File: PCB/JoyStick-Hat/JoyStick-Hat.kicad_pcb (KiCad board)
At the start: 2 copper layers, 65 x 100 mm, 108 parts, among them J1 20021121-00010C4LF, J10 Conn_01x02_Pin, J11 Conn_01x02_Pin, J12 Conn_01x02_Pin, J13 Conn_01x02_Pin, J14 Conn_01x03_Pin, J15 Conn_01x03_Pin, J16 Conn_01x06, J2 BU2032SM-JJ-GTR, J3 0675031020, J4 Conn_02x14_Counter_Clockwise, J5 Conn_02x14_Counter_Clockwise, J6 1757242, J7 Raspberry_Pi_2_3, J8 Conn_01x04_Pin, J9 Conn_01x04_Pin, M1 D24V22F12, M2 D24V22F5, M3 D24V22F3, SW1 TL3301NF260QG, U1 STM32F446VETx, U2 TLC5947DAP, U3 TLC5947DAP, U4 MAX3535ECWI+T, X1 ABM3B-8.000MHZ-B2-T, X2 ABS07-32.768KHZ-9-T

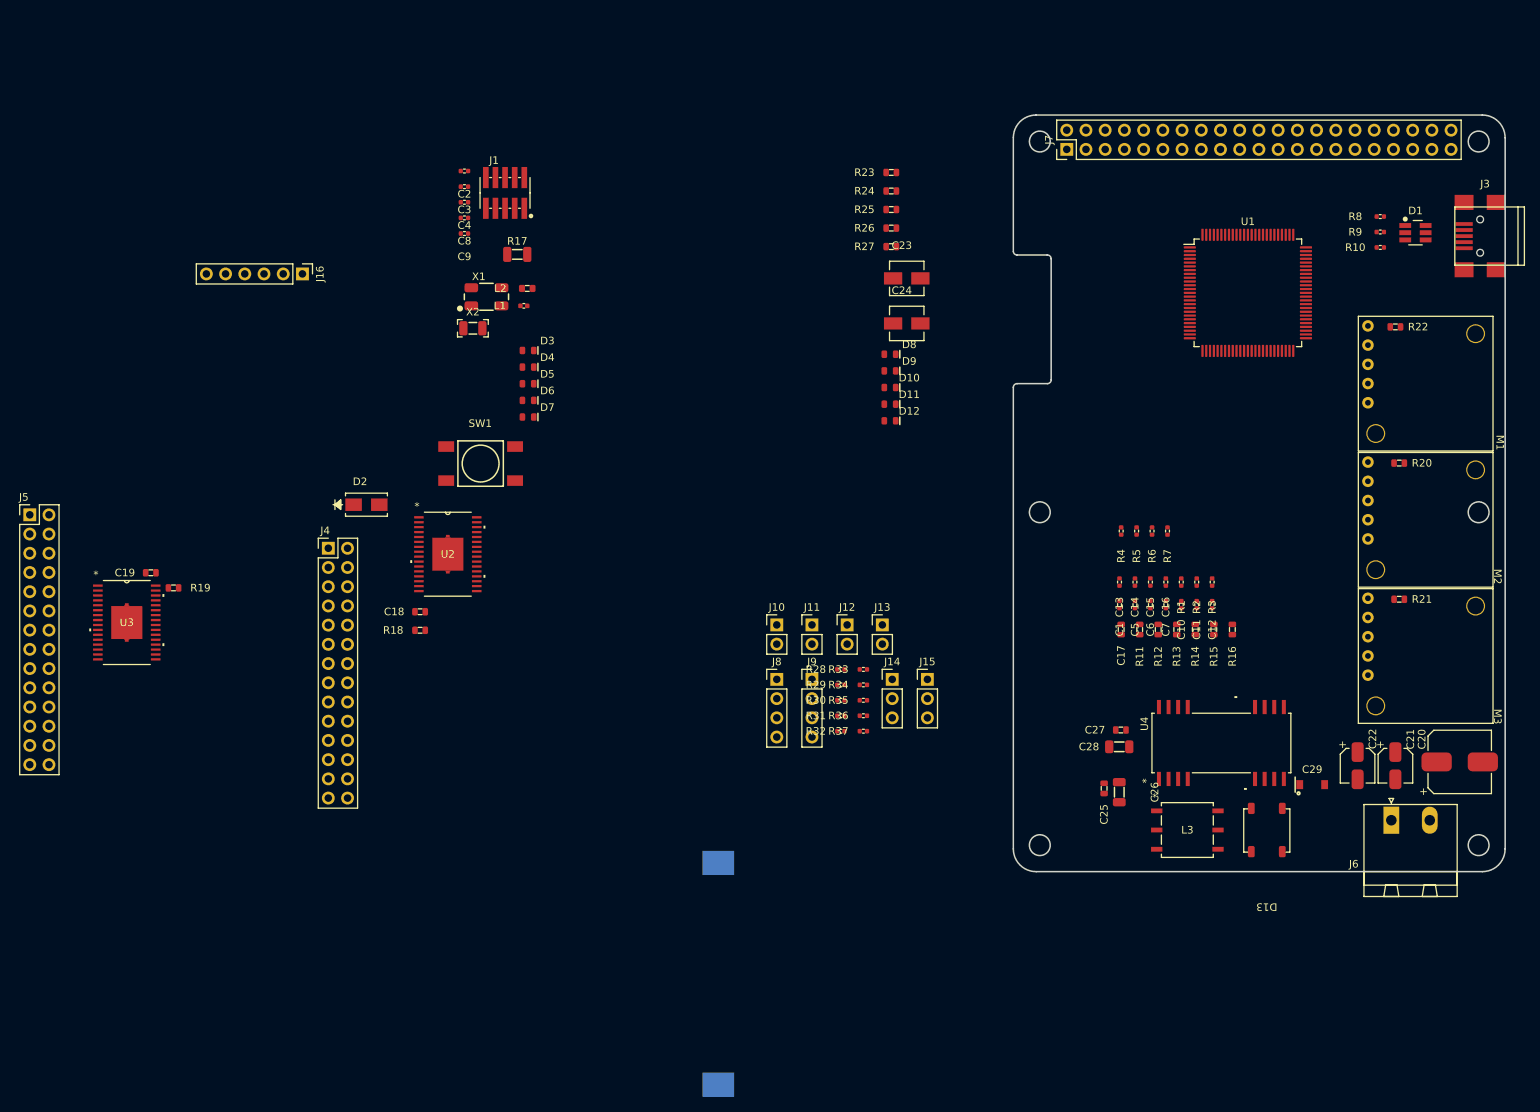
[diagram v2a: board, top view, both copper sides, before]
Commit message: Design Rules, Component Placement. Features Dropped
Added design rules for OSHPark.com to PCB, Most components placed roughly for whole board more to follow and more tweaks,. Features were dropped/rearanged. USB for STM32 dropped as its not necessary. LED driver and LEDs will be on separate board and SPI will run through cabling via differential transceiver that has yet to be added to schematic.
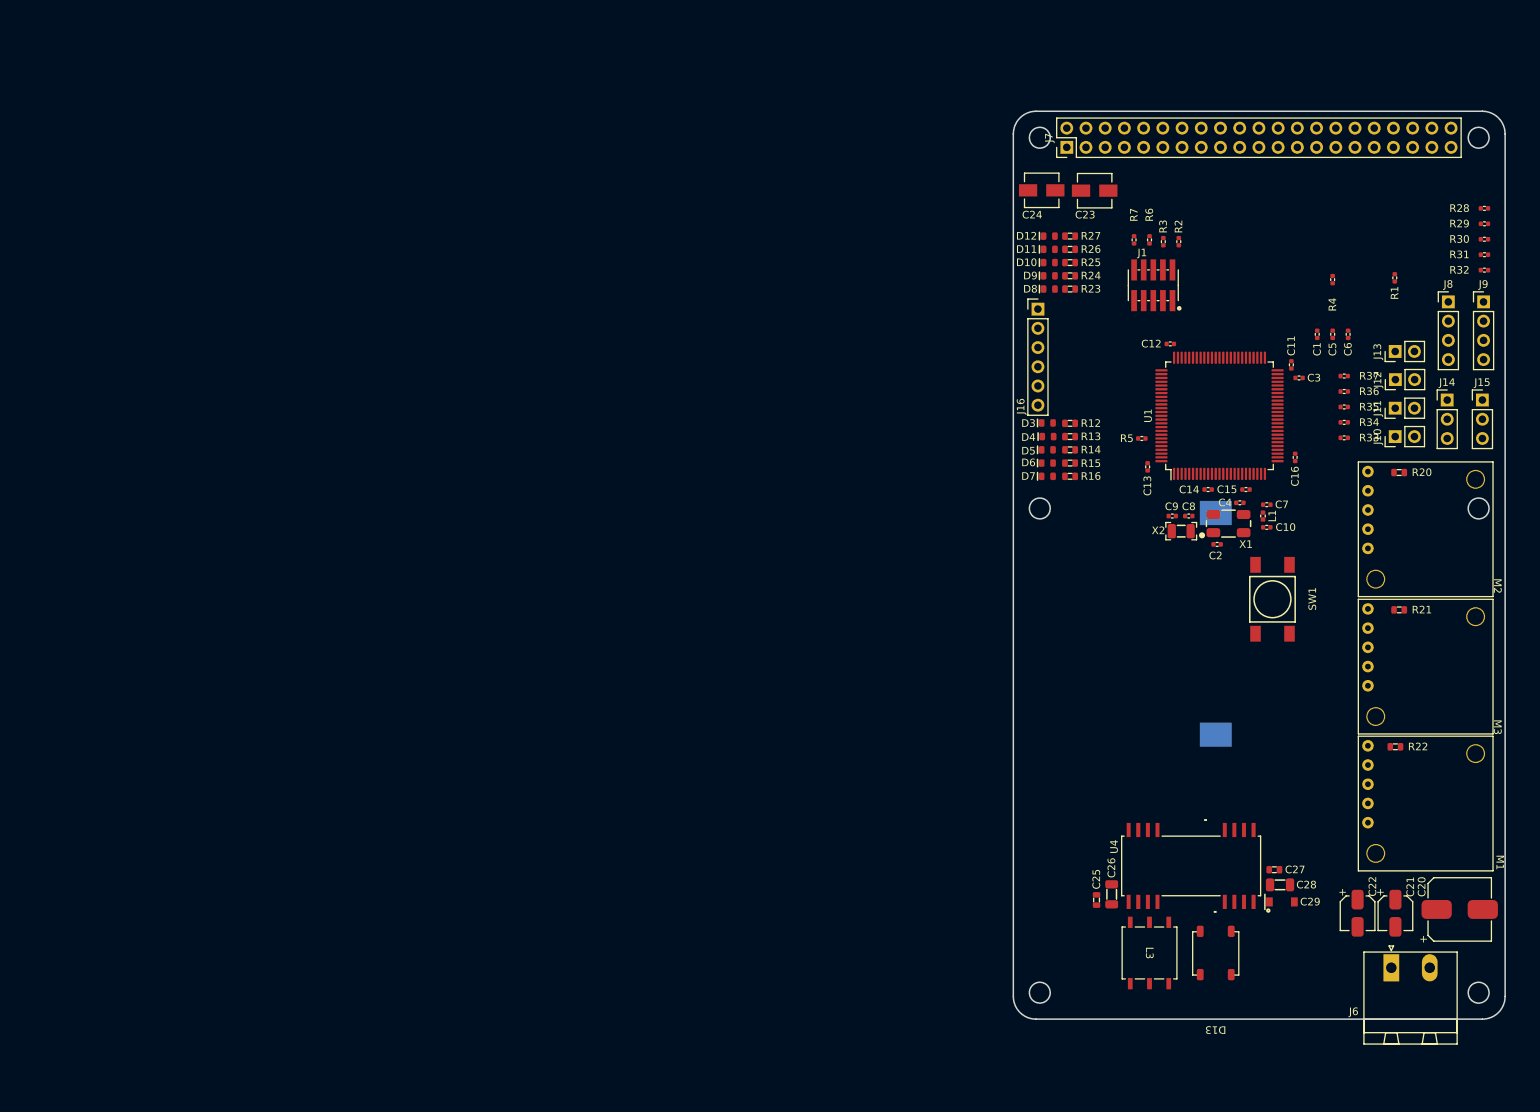
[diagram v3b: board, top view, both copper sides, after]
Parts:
- removed C17: C0603X103K1RAC3316, AVR-KiCAD-Lib-Capacitors:C0603
- removed C18, C19: CL10B104JB8NNNC, AVR-KiCAD-Lib-Capacitors:C0603
- removed D1: ESDA6V1BC6, AVR-KiCAD-Lib-ICs:SOT-23-6_Handsoldering
- removed D2: SMAJ30CA, AVR-KiCAD-Lib-Diodes:SMAJ30CA
- removed J3: 0675031020, AVR-KiCAD-Lib-Connectors:USB_Mini-B
- removed J4, J5: Conn_02x14_Counter_Clockwise, Connector_PinHeader_2.54mm:PinHeader_2x14_P2.54mm_Vertical
- removed L2: MI0603K300R-10, AVR-KiCAD-Lib-Inductors:MI0603K300R-10
- removed R10: RC0402FR-0710KL, AVR-KiCAD-Lib-Resistors:R0402
- removed R11: RC0603FR-0747KL, AVR-KiCAD-Lib-Resistors:R0603
- removed R17: RC1206FR-071ML, AVR-KiCAD-Lib-Resistors:R1206
- removed R18, R19: RMCF0603FT2K61, AVR-KiCAD-Lib-Resistors:R0603
- removed R8, R9: RC0402FR-0722RL, AVR-KiCAD-Lib-Resistors:R0402
- removed U2, U3: TLC5947DAP, AVR-KiCAD-Lib-ICs:DAP32_4P36X4P11
- moved C3 113.2 mm to (237.8, 74.8)
- moved C2 111.1 mm to (226.9, 96.8)
- moved C4 109.9 mm to (229.9, 91.2), turned to 180 degrees
- moved SW1 106.2 mm to (234.2, 104.0), turned to -90 degrees
- moved R28 104.6 mm to (262.3, 52.3)
- moved R29 104.6 mm to (262.3, 54.4)
- moved R30 104.6 mm to (262.3, 56.4)
- moved R31 104.6 mm to (262.3, 58.5)
- moved R32 104.6 mm to (262.3, 60.5)
- moved C8 103.5 mm to (223.2, 93.0), turned to 180 degrees
- moved X1 102.6 mm to (228.4, 94.0)
- moved J8 101.8 mm to (257.5, 64.7)
- moved J9 101.8 mm to (262.1, 64.7)
- moved L1 101.6 mm to (233.0, 93.0), turned to 90 degrees
- moved C9 100.7 mm to (221.0, 93.0)
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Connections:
- C11 pad 1: Net-(C11-Pad1) -> +3V3
- C12 pad 1: Net-(C11-Pad1) -> +3V3
- C13 pad 1: Net-(C11-Pad1) -> +3V3
- C14 pad 1: Net-(C11-Pad1) -> +3V3
- C15 pad 1: Net-(C11-Pad1) -> +3V3
- C16 pad 1: Net-(C11-Pad1) -> +3V3
- U1 pad 100: Net-(C11-Pad1) -> +3V3
- U1 pad 11: Net-(C11-Pad1) -> +3V3
- U1 pad 19: Net-(C11-Pad1) -> +3V3
- U1 pad 28: Net-(C11-Pad1) -> +3V3
- U1 pad 29: /LED-Driver-Power/LED_DRIVER_XLAT -> /STM32F446RET6-MCU/LED_DRIVER_XLAT
- U1 pad 30: /LED-Driver-Power/LED_DRIVER_SCLK -> /STM32F446RET6-MCU/LED_DRIVER_SCLK
- U1 pad 31: /LED-Driver-Speed/LED_DRIVER_BLANK2 -> /STM32F446RET6-MCU/LED_DRIVER_BLANK2
- U1 pad 32: /LED-Driver-Power/LED_DRIVER_MOSI -> /STM32F446RET6-MCU/LED_DRIVER_MOSI
- U1 pad 33: /LED-Driver-Power/LED_DRIVER_BLANK -> /STM32F446RET6-MCU/LED_DRIVER_BLANK
- U1 pad 34: /LED-Driver-Speed/LED_DRIVER_XLAT2 -> /STM32F446RET6-MCU/LED_DRIVER_XLAT2
- U1 pad 50: Net-(C11-Pad1) -> +3V3
- U1 pad 53: /STM32F446RET6-MCU/MCU_D- -> unconnected-(U1-PB14-Pad53)
- U1 pad 54: /STM32F446RET6-MCU/MCU_D+ -> unconnected-(U1-PB15-Pad54)
- U1 pad 75: Net-(C11-Pad1) -> +3V3
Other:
- board size 65 x 100 mm -> 65 x 120 mm
- copper layers 2 -> 4

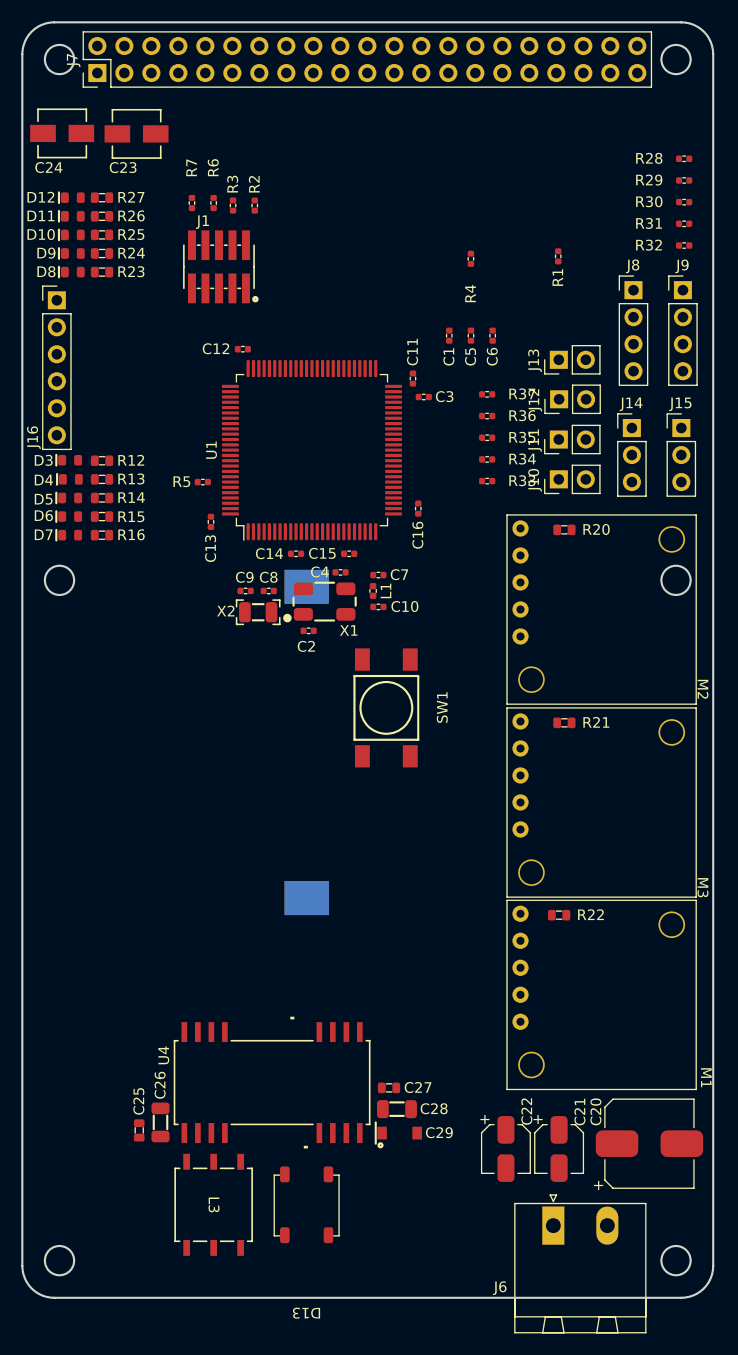
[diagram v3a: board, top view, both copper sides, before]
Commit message: Board Tweaks and progress
Made progress with baord. Adjusted the position of RPi header to be correct and absolute. Changed location of regulator modules and power input capacitors. Added 3D models missing from the larger components. Changed connectors and positions for just about everything. Added connnector for LED driver duagher board .
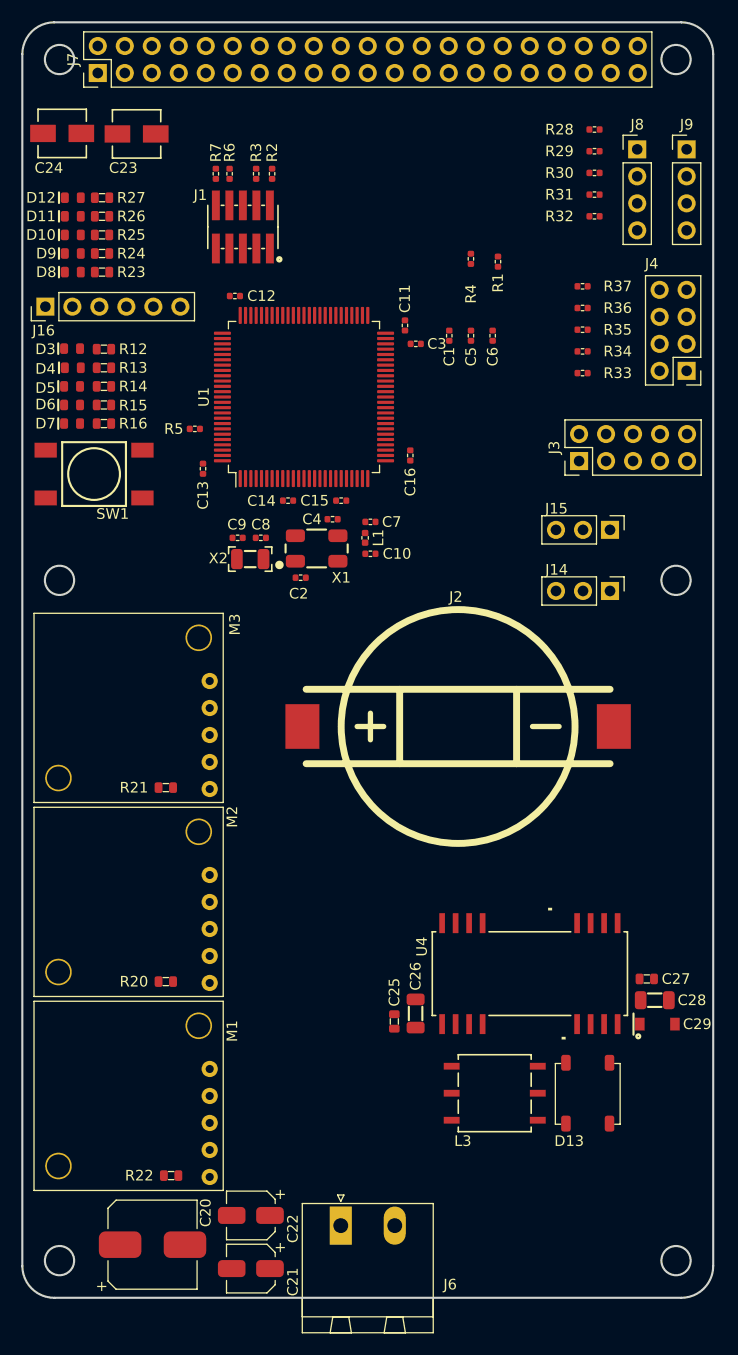
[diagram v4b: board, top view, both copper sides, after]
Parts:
- removed J10, J11, J12, J13: Conn_01x02_Pin, Connector_PinHeader_2.54mm:PinHeader_1x02_P2.54mm_Vertical
- added J3: Conn_02x05_Odd_Even, Connector_PinHeader_2.54mm:PinHeader_2x05_P2.54mm_Vertical, F.Cu at (252.4, 80.8)
- added J4: Conn_02x04_Odd_Even, Connector_PinHeader_2.54mm:PinHeader_2x04_P2.54mm_Vertical, F.Cu at (262.5, 72.3)
- J2: moved to F.Cu
- J7: footprint Connector_PinHeader_2.54mm:PinHeader_2x21_P2.54mm_Vertical -> AVR-KiCAD-Lib-Connectors:PinHeader_2x21_P2.54mm_Vertical
- moved R20 56.7 mm to (213.5, 129.8), turned to 0 degrees
- moved M2 51.8 mm to (217.6, 129.9), turned to 90 degrees
- moved C20 47.7 mm to (212.2, 154.5)
- moved R22 44.0 mm to (214.0, 148.0), turned to 180 degrees
- moved M1 38.3 mm to (217.6, 148.1), turned to 90 degrees
- moved R21 38.0 mm to (213.5, 111.5), turned to 0 degrees
- moved SW1 35.2 mm to (206.8, 82.0), turned to 0 degrees
- moved C21 31.1 mm to (221.5, 156.8), turned to 180 degrees
- moved M3 29.9 mm to (217.6, 111.6), turned to 90 degrees
- moved D13 28.5 mm to (253.2, 140.2)
- moved L3 28.5 mm to (244.4, 140.2), turned to 0 degrees
- moved C27 26.3 mm to (258.8, 129.5)
- moved C28 26.3 mm to (259.5, 131.5)
- moved C29 26.3 mm to (259.8, 133.8)
- moved U4 26.3 mm to (247.8, 129.0)
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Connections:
- L3 pad 1: Net-(U4-ST1) -> Net-(U4-ST2)
- L3 pad 3: Net-(U4-ST2) -> Net-(U4-ST1)
- L3 pad 4: Net-(D13-Pad2) -> Net-(D13-Pad1)
- L3 pad 6: Net-(D13-Pad1) -> Net-(D13-Pad2)
